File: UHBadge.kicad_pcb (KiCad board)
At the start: 2 copper layers, 70 x 117.6 mm, 80 parts, among them J1 Conn_01x03_MountingPin, J2 Conn_01x10_MountingPin, J3 LEMO2, P1 USB_C_Plug_USB2.0, Q1 Si1308EDL, SW1 Boot, SW2 Run, SW3 Up, SW4 Down, SW5 Left, SW6 Right, U1 RP2350A, U2 MCP73871, U3 W25Q128JVS, U4 SRV05-4, U5 Conn, U6 ST25DV64K-JFR6D3, Y1 ABM8-272-T3

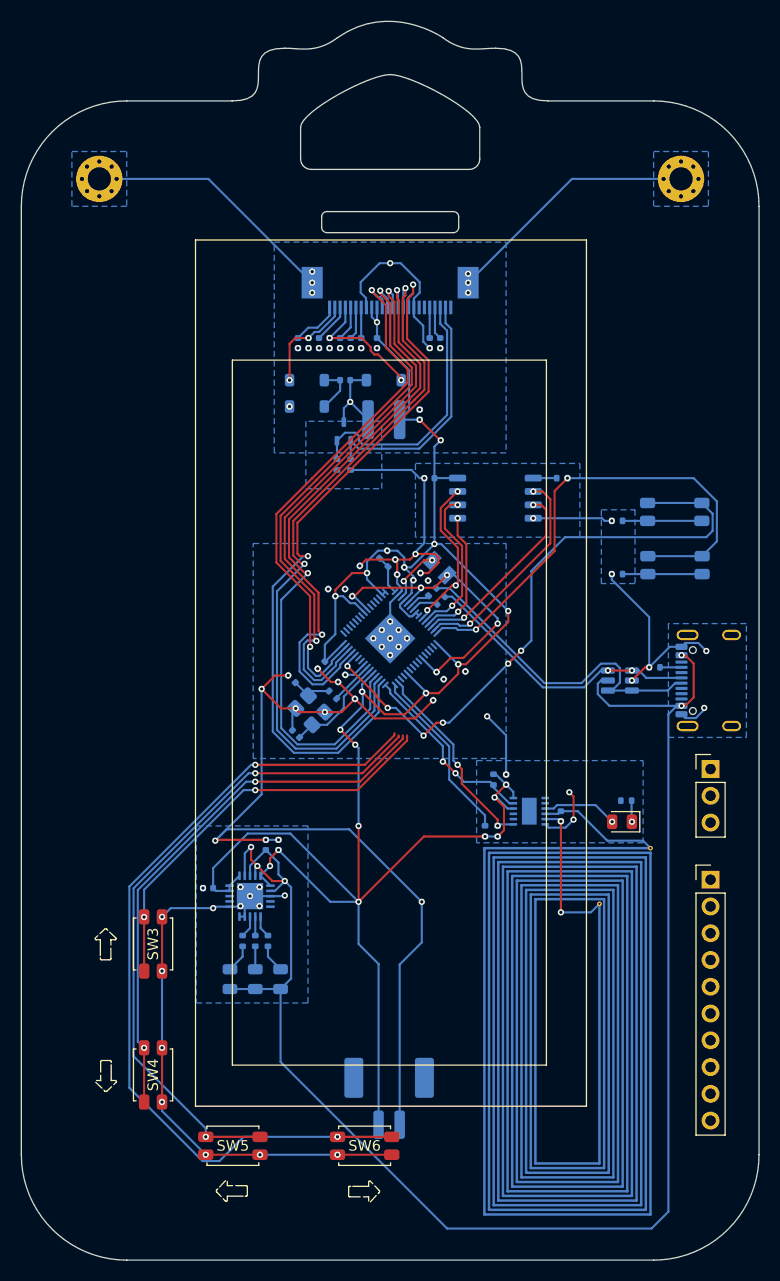
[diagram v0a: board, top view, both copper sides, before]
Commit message: Fixed the position of the GPIO and SWD pins.
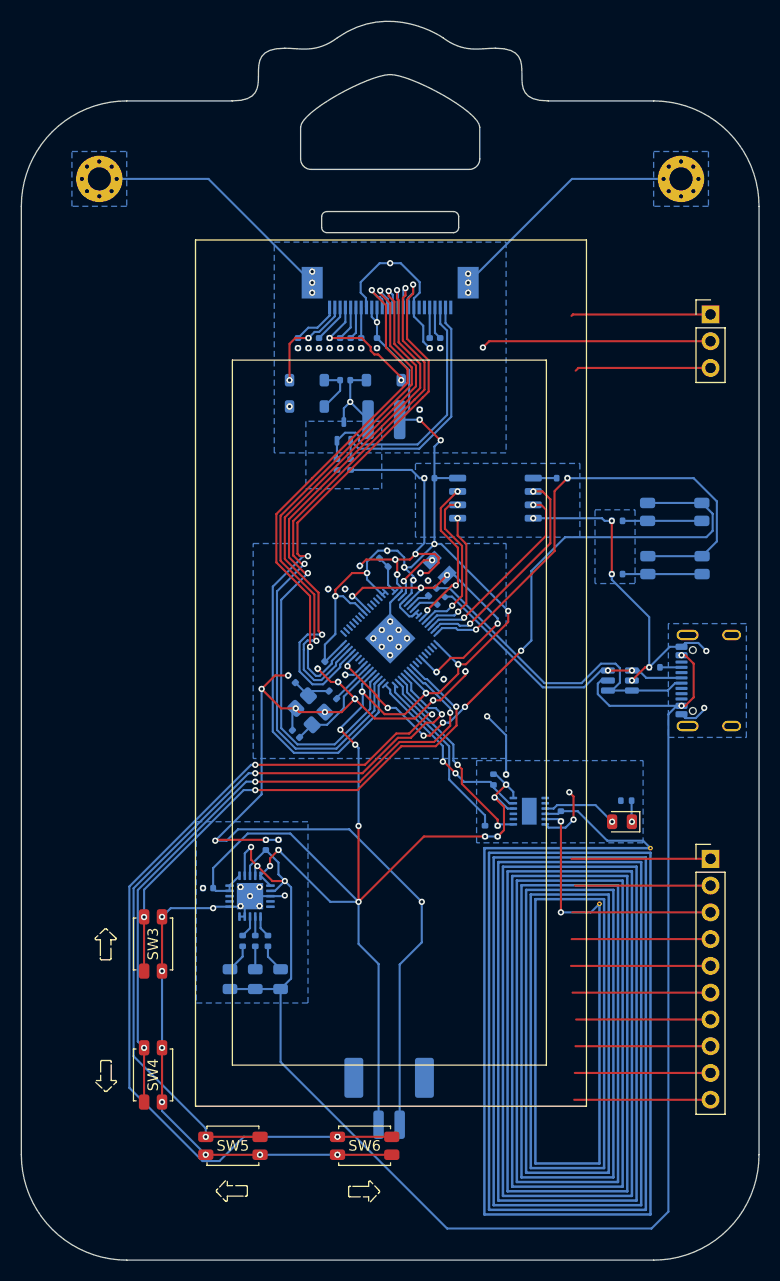
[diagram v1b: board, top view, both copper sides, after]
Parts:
- moved J1 43.1 mm to (165.4, 70.3)
- moved J2 1.98 mm to (165.4, 121.9)
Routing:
- net -BATT: track 291.4 -> 335.6 mm, vias 77 -> 78
- net SWCLK: track 0.00 -> 13.3 mm
- net GPIO3: track 0.00 -> 13.2 mm
- net +3V3: track 213.2 -> 226.4 mm
- net GPIO2: track 0.00 -> 13.2 mm
- net GPIO1: track 0.00 -> 13.1 mm
- net GPIO4: track 0.00 -> 13.1 mm
- net SWDIO: track 0.00 -> 12.9 mm
- net ADC1: track 0.00 -> 12.9 mm
- net GPIO0: track 0.00 -> 12.9 mm
- net ADC0: track 0.00 -> 12.8 mm
- net GPIO5: track 0.00 -> 12.8 mm
- net UP: track 39.1 -> 51.3 mm, vias 2 -> 3
- net DOWN: track 51.8 -> 63.5 mm, vias 2 -> 3
- net LEFT: track 62.8 -> 73.2 mm, vias 2 -> 3
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
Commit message: UHBadge - Finished the connections between the components.
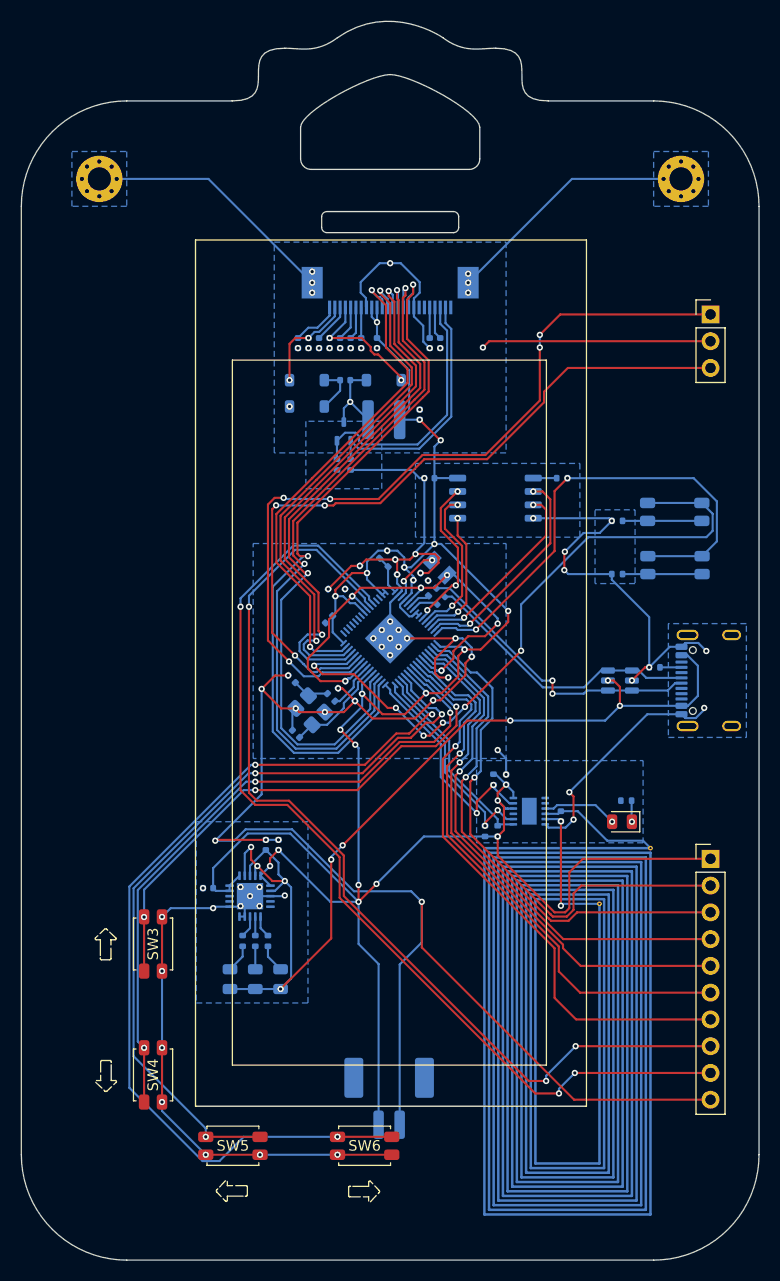
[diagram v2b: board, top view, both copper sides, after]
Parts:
- moved C11 4.40 mm to (129.2, 99.2)
- moved C7 1.52 mm to (142.4, 102.4)
- moved C5 0.60 mm to (130.4, 105.4)
- moved C6 0.48 mm to (140.2, 104.4)
- moved R10 0.29 mm to (129.4, 106.6)
- moved C12 0.20 mm to (132.0, 106.6)
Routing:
- net ADC1: track 12.9 -> 95.2 mm, vias 0 -> 3
- net ADC0: track 12.8 -> 93.5 mm, vias 0 -> 3
- net SWCLK: track 13.3 -> 77.0 mm, vias 0 -> 5
- net -BATT: track 335.6 -> 393.3 mm, vias 78 -> 79
- net SWDIO: track 12.9 -> 69.8 mm, vias 0 -> 3
- net USB_C_VBUS: track 149.8 -> 97.6 mm, vias 5 -> 9
- net GPIO5: track 12.8 -> 55.9 mm, vias 0 -> 1
- net GPIO4: track 13.1 -> 53.3 mm, vias 0 -> 1
- net GPIO3: track 13.2 -> 50.7 mm, vias 0 -> 1
- net GPIO0: track 12.9 -> 50.1 mm, vias 0 -> 1
- net GPIO2: track 13.2 -> 49.3 mm, vias 0 -> 1
- net GPIO1: track 13.1 -> 48.6 mm, vias 0 -> 1
- net +1V1: track 32.8 -> 46.0 mm
- net +3V3: track 226.4 -> 237.2 mm
- net RUN: track 59.0 -> 63.8 mm
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
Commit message: Added two new mounting holes. Fixed the NFC footprint. Started working on the design.
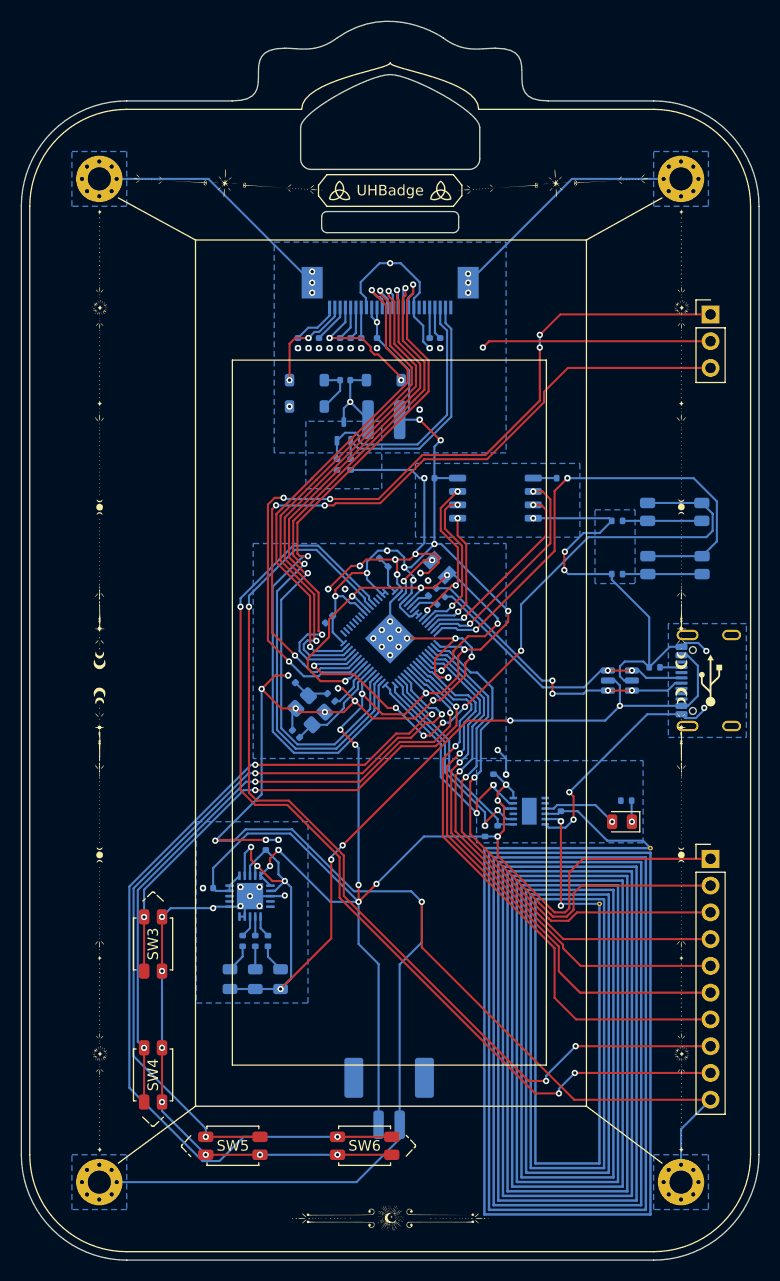
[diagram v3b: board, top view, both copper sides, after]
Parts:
- added G***: LOGO, LOGO, F.Cu at (130.2, 58.5)
- added G***: LOGO, LOGO, F.Cu at (162.6, 88.5)
- added G***: LOGO, LOGO, F.Cu at (162.6, 105.0)
- added G***: LOGO, LOGO, F.Cu at (107.4, 88.6)
- added G***: LOGO, LOGO, F.Cu at (119.4, 57.8)
- added G***: LOGO, LOGO, F.Cu at (162.6, 69.6)
- added G***: LOGO, LOGO, F.Cu at (162.6, 121.6)
- added G***: LOGO, LOGO, F.Cu at (150.8, 57.8)
- added G***: LOGO, LOGO, B.Cu at (151.8, 137.4)
- added G***: LOGO, LOGO, F.Cu at (107.4, 69.6)
- added G***: LOGO, LOGO, F.Cu at (165.4, 105.0)
- added G***: LOGO, LOGO, F.Cu at (135.0, 156.0)
- added G***: LOGO, LOGO, F.Cu at (107.4, 105.0)
- added G***: LOGO, LOGO, F.Cu at (139.8, 58.5)
- added G***: LOGO, LOGO, F.Cu at (107.4, 140.4)
- added G***: LOGO, LOGO, F.Cu at (162.6, 140.4)
- added G***: LOGO, LOGO, F.Cu at (107.4, 121.6)
- added H3: MountingHole_Pad, MountingHole:MountingHole_2.2mm_M2_Pad_Via, F.Cu at (162.6, 152.6)
- added H4: MountingHole_Pad, MountingHole:MountingHole_2.2mm_M2_Pad_Via, F.Cu at (107.4, 152.6)
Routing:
- net -BATT: track 393.3 -> 437.2 mm, vias 79 -> 76
- net USB_C_VBUS: vias 9 -> 8
- net USB_C_D+: vias 0 -> 2
- net USB_C_D-: vias 2 -> 4
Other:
- board text added: "LiPo Recharger"
- board text added: "RP2350"
- board text added: "UHBadge"

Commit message: Remade the whole design.
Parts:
- removed the G*** at (130.2, 58.5)
- removed the G*** at (162.6, 88.5)
- removed the G*** at (162.6, 105.0)
- removed the G*** at (107.4, 88.6)
- removed the G*** at (119.4, 57.8)
- removed the G*** at (162.6, 69.6)
- removed the G*** at (162.6, 121.6)
- removed the G*** at (150.8, 57.8)
- removed the G*** at (107.4, 69.6)
- removed the G*** at (135.0, 156.0)
- removed the G*** at (107.4, 105.0)
- removed the G*** at (139.8, 58.5)
- removed the G*** at (107.4, 140.4)
- removed the G*** at (162.6, 140.4)
- removed the G*** at (107.4, 121.6)
- added G***: LOGO, LOGO, F.Cu at (114.4, 114.2)
- added G***: LOGO, LOGO, F.Cu at (130.2, 58.5)
- added G***: LOGO, LOGO, F.Cu at (139.8, 58.6)
- added G***: LOGO, LOGO, B.Cu at (112.2, 72.0)
- G***: moved to B.Cu
- moved G*** 7.20 mm to (165.4, 112.2), turned to 0 degrees
- moved G*** 1.00 mm to (151.8, 138.4)
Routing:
- net (no net): vias 0 -> 11
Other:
- board text added: "//"
- board text added: "///"
- board text added: "//////////"
- board text added: "Better tools for a better future."
- board text added: "D e v e l o p e r"
- board text added: "H a c k e r"
- board text added: "O p e n S o u r c e"
- board text added: "Open Source Open Hardware"
- board text added: "UHB"
- board text added: "Universal Hacker Badge"
- board text added: "\\\"
- board text added: "hack. learn. love."
- board text added: "||||||"

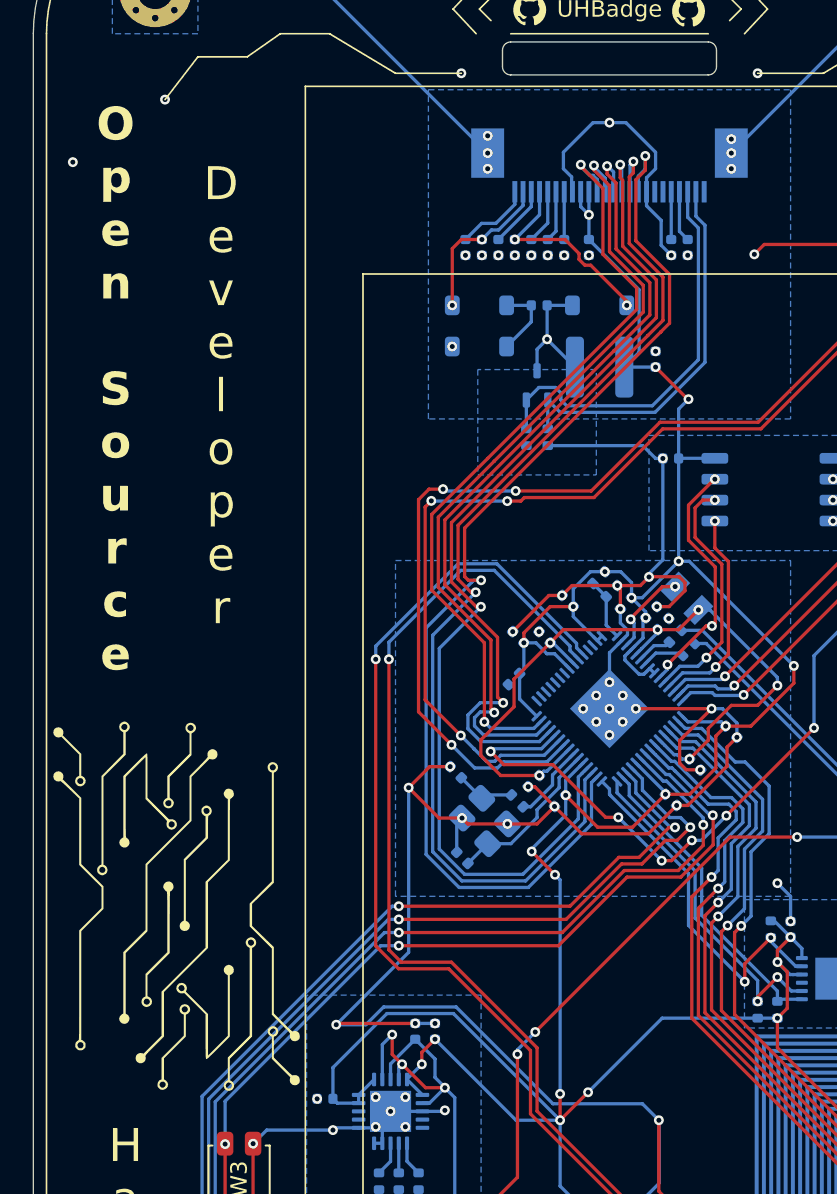
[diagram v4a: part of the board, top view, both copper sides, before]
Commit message: Added the Pi Radio Module 2.
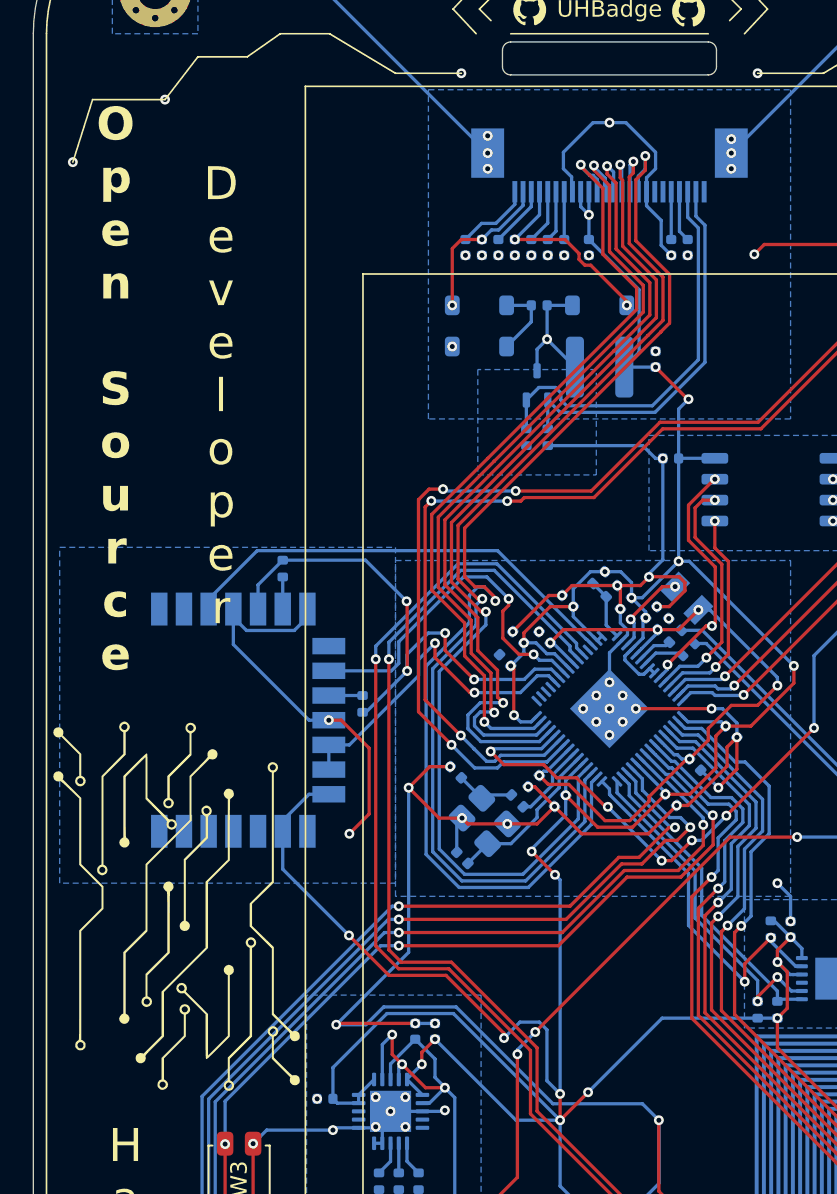
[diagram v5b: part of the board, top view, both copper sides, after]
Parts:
- added R18: 470Ω, Resistor_SMD:R_0402_1005Metric, B.Cu at (115.2, 92.5)
- added R19: 10kΩ, Resistor_SMD:R_0402_1005Metric, B.Cu at (120.0, 100.7)
- added U7: Radio Module 2, CustomFootprints:rpi_rmc20452t, B.Cu at (110.2, 101.7)
- moved C11 1.26 mm to (128.7, 98.1), turned to 135 degrees
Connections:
- U1 pad 35: unconnected-(U1-GPIO23-Pad35) -> GPIO23
- U1 pad 36: unconnected-(U1-GPIO24-Pad36) -> GPIO24
- U1 pad 37: unconnected-(U1-GPIO25-Pad37) -> GPIO25
- U1 pad 43: unconnected-(U1-GPIO29/ADC3-Pad43) -> GPIO29
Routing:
- net GPIO24: track 0.00 -> 33.3 mm, vias 0 -> 4
- net +3V3: track 237.2 -> 270.4 mm, vias 23 -> 27
- net GPIO29: track 0.00 -> 27.5 mm
- net -BATT: track 437.2 -> 461.6 mm, vias 76 -> 78
- net GPIO25: track 0.00 -> 21.8 mm, vias 0 -> 2
- net GPIO23: track 0.00 -> 20.7 mm, vias 0 -> 2
- net E-INK_BUSY: track 69.0 -> 71.3 mm
- net Net-(U7-nIRQ): track 0.00 -> 2.05 mm
- net Net-(U7-DO): track 0.00 -> 1.95 mm
- net +1V1: track 46.0 -> 45.3 mm
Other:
- board text added: "Pi Radio Module 2"
